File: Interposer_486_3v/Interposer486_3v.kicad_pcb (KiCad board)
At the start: 2 copper layers, 48.3 x 81.3 mm, 244 parts, among them CN1 +5v External, J1 WB/~WT, J2 CLKMUL, J3 V Select, U1 LT1085-ADJ

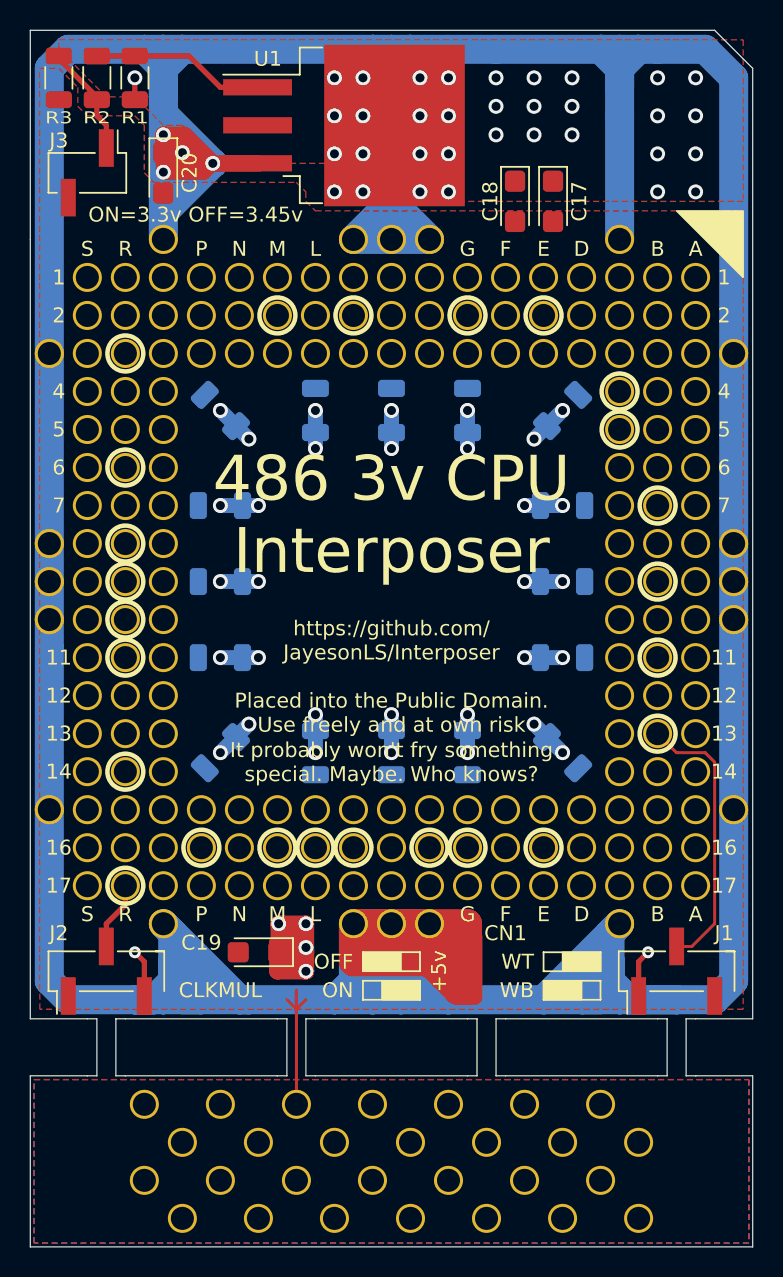
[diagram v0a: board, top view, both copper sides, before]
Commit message: Remove drill template from 486 3v interposer.
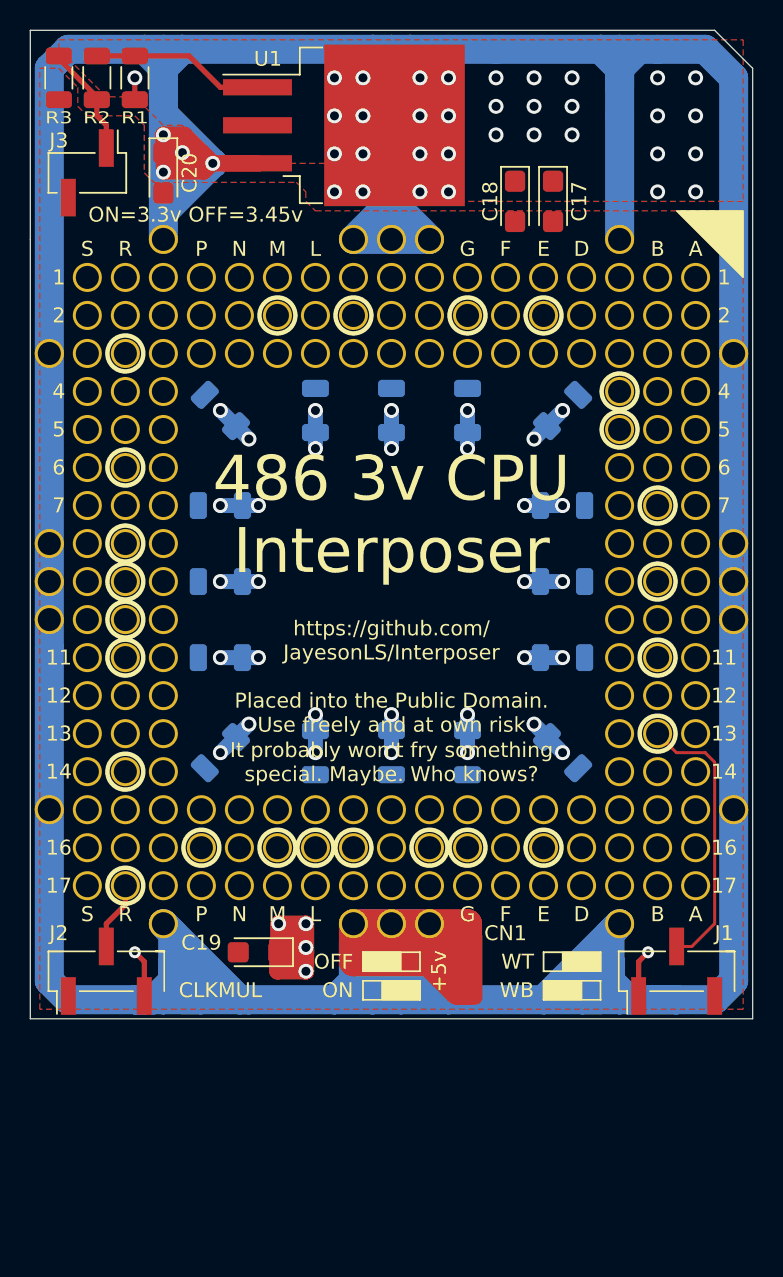
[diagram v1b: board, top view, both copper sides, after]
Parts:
- removed HDT1, HDT10, HDT11, HDT12, HDT13, HDT14, HDT15, HDT16, HDT17, HDT18, HDT19, HDT2, HDT20, HDT21, HDT22, HDT23, HDT24, HDT25, HDT26, HDT27, HDT28, HDT3, HDT4, HDT5, HDT6, HDT7, HDT8, HDT9: ???, 00Custom:MachinePinHole
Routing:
- net VSS: track 50.8 -> 41.3 mm
- removed copper zone on B.Cu, net VSS
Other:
- board size 48.3 x 81.3 mm -> 48.3 x 66 mm
